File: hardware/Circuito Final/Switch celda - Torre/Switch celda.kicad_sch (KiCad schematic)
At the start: 28 parts, among them Q1 MMBT2222A, Q2 MMBT2907A, Q3 MMBT2222A

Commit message: Subida de la versión torrecita
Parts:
- removed J_In_Out_1: Conn_01x05_Socket, Connector_PinSocket_2.54mm:PinSocket_1x05_P2.54mm_Vertical, symbol Connector:Conn_01x05_Socket
- added J_In_Out_1: Conn_01x06_Socket, Connector_PinSocket_2.54mm:PinSocket_1x06_P2.54mm_Vertical, symbol Connector:Conn_01x06_Socket
- added TPgnd1, TPgnd2: TP_gnd, Connector_PinHeader_2.54mm:PinHeader_1x01_P2.54mm_Vertical, symbol Connector:TestPoint
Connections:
- net 0: now also J_In_Out_1.2 (Pin_2), J_In_Out_1.4 (Pin_4), TPgnd1.1, TPgnd2.1
- net Vcc: now also J_In_Out_1.5 (Pin_5)
- net Vcell_banco: now also J_In_Out_1.3 (Pin_3)
- net bus_neg: now also J_In_Out_1.1 (Pin_1)
- net bus_pos: now also J_In_Out_1.6 (Pin_6)

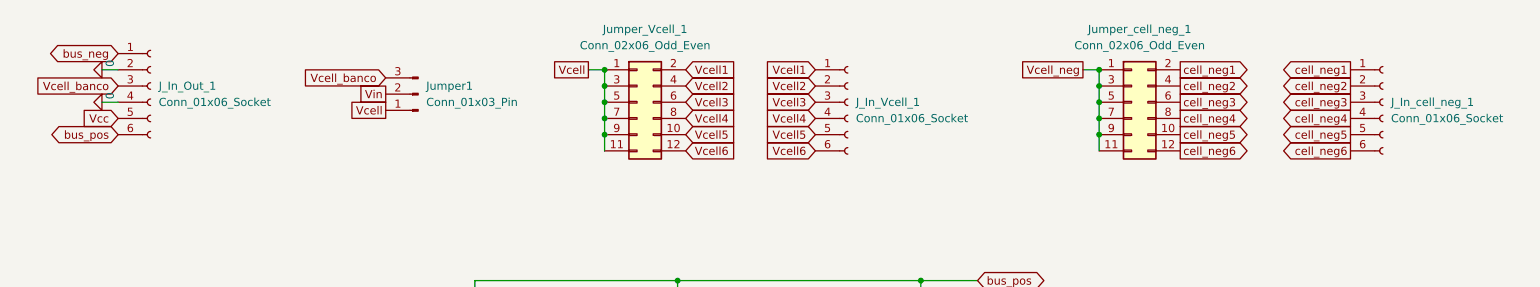
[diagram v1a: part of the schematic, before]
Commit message: Se duplican dos de las 3 tiras de pines del circuito de celda topología torre
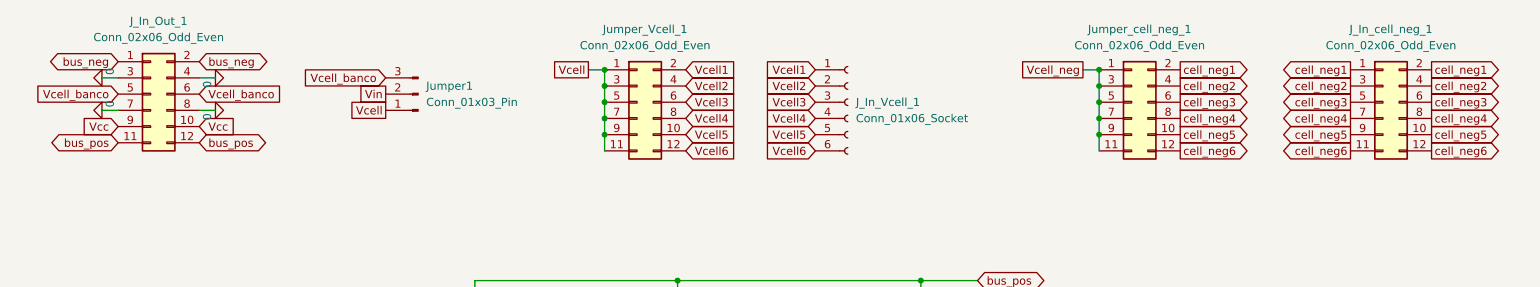
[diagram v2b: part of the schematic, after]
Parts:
- removed J_In_Out_1, J_In_cell_neg_1: Conn_01x06_Socket, Connector_PinSocket_2.54mm:PinSocket_1x06_P2.54mm_Vertical, symbol Connector:Conn_01x06_Socket
- added J_In_Out_1, J_In_cell_neg_1: Conn_02x06_Odd_Even, Connector_PinSocket_2.54mm:PinSocket_2x06_P2.54mm_Vertical, symbol Connector_Generic:Conn_02x06_Odd_Even
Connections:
- net 0: now also J_In_Out_1.3 (Pin_3), J_In_Out_1.4 (Pin_4), J_In_Out_1.7 (Pin_7), J_In_Out_1.8 (Pin_8)
- net Vcc: now also J_In_Out_1.10 (Pin_10), J_In_Out_1.9 (Pin_9)
- net Vcell_banco: now also J_In_Out_1.5 (Pin_5), J_In_Out_1.6 (Pin_6)
- net bus_neg: now also J_In_Out_1.1 (Pin_1), J_In_Out_1.2 (Pin_2)
- net bus_pos: now also J_In_Out_1.11 (Pin_11), J_In_Out_1.12 (Pin_12)
- net cell_neg1: now also J_In_cell_neg_1.1 (Pin_1), J_In_cell_neg_1.2 (Pin_2)
- net cell_neg2: now also J_In_cell_neg_1.3 (Pin_3), J_In_cell_neg_1.4 (Pin_4)
- net cell_neg3: now also J_In_cell_neg_1.5 (Pin_5), J_In_cell_neg_1.6 (Pin_6)
- net cell_neg4: now also J_In_cell_neg_1.7 (Pin_7), J_In_cell_neg_1.8 (Pin_8)
- net cell_neg5: now also J_In_cell_neg_1.10 (Pin_10), J_In_cell_neg_1.9 (Pin_9)
- net cell_neg6: now also J_In_cell_neg_1.11 (Pin_11), J_In_cell_neg_1.12 (Pin_12)

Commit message: Cambios al circuito de la celda en modo torre: clearance de 0.5mm (en lugar de la mínima), buses de potencia de 1.5mm (en lugar de 1mm) y resistores SMD de tamaño 1206 (en lugar de 0603)
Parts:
- F1: footprint Fuse:Fuse_0603_1608Metric_Pad1.05x0.95mm_HandSolder -> Fuse:Fuse_1206_3216Metric_Pad1.42x1.75mm_HandSolder
- R1, R2, R3, R4, R5, R6, RLED1, RLED2: footprint Resistor_SMD:R_0603_1608Metric_Pad0.98x0.95mm_HandSolder -> Resistor_SMD:R_1206_3216Metric_Pad1.30x1.75mm_HandSolder
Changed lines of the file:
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@@
 			)
 		)
-		(property "Footprint" "Resistor_SMD:R_0603_1608Metric_Pad0.98x0.95mm_HandSolder"
+		(property "Footprint" "Resistor_SMD:R_1206_3216Metric_Pad1.30x1.75mm_HandSolder"
 			(at 67.564 95.504 90)
 			(effects
@@
 			)
 		)
-		(property "Footprint" "Fuse:Fuse_0603_1608Metric_Pad1.05x0.95mm_HandSolder"
+		(property "Footprint" "Fuse:Fuse_1206_3216Metric_Pad1.42x1.75mm_HandSolder"
 			(at 156.21 63.5 0)
 			(effects
@@
 			)
 		)
-		(property "Footprint" "Resistor_SMD:R_0603_1608Metric_Pad0.98x0.95mm_HandSolder"
+		(property "Footprint" "Resistor_SMD:R_1206_3216Metric_Pad1.30x1.75mm_HandSolder"
 			(at 85.344 83.566 90)
 			(effects
@@
 			)
 		)
-		(property "Footprint" "Resistor_SMD:R_0603_1608Metric_Pad0.98x0.95mm_HandSolder"
+		(property "Footprint" "Resistor_SMD:R_1206_3216Metric_Pad1.30x1.75mm_HandSolder"
 			(at 85.344 64.516 90)
 			(effects
@@
 			)
 		)
-		(property "Footprint" "Resistor_SMD:R_0603_1608Metric_Pad0.98x0.95mm_HandSolder"
+		(property "Footprint" "Resistor_SMD:R_1206_3216Metric_Pad1.30x1.75mm_HandSolder"
 			(at 101.854 119.634 90)
 			(effects
@@
 			)
 		)
-		(property "Footprint" "Resistor_SMD:R_0603_1608Metric_Pad0.98x0.95mm_HandSolder"
+		(property "Footprint" "Resistor_SMD:R_1206_3216Metric_Pad1.30x1.75mm_HandSolder"
 			(at 214.884 100.584 90)
 			(effects
@@
 			)
 		)
-		(property "Footprint" "Resistor_SMD:R_0603_1608Metric_Pad0.98x0.95mm_HandSolder"
+		(property "Footprint" "Resistor_SMD:R_1206_3216Metric_Pad1.30x1.75mm_HandSolder"
 			(at 117.094 87.376 90)
 			(effects
@@
 			)
 		)
-		(property "Footprint" "Resistor_SMD:R_0603_1608Metric_Pad0.98x0.95mm_HandSolder"
+		(property "Footprint" "Resistor_SMD:R_1206_3216Metric_Pad1.30x1.75mm_HandSolder"
 			(at 227.584 89.916 90)
 			(effects
@@
 			)
 		)
-		(property "Footprint" "Resistor_SMD:R_0603_1608Metric_Pad0.98x0.95mm_HandSolder"
+		(property "Footprint" "Resistor_SMD:R_1206_3216Metric_Pad1.30x1.75mm_HandSolder"
 			(at 117.094 106.426 90)
 			(effects

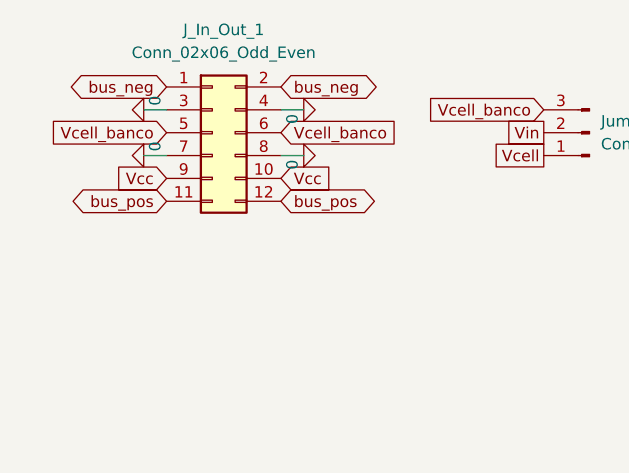
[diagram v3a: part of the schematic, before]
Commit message: Update menor de orden de señales en la entrada (VCC por bus_pos)
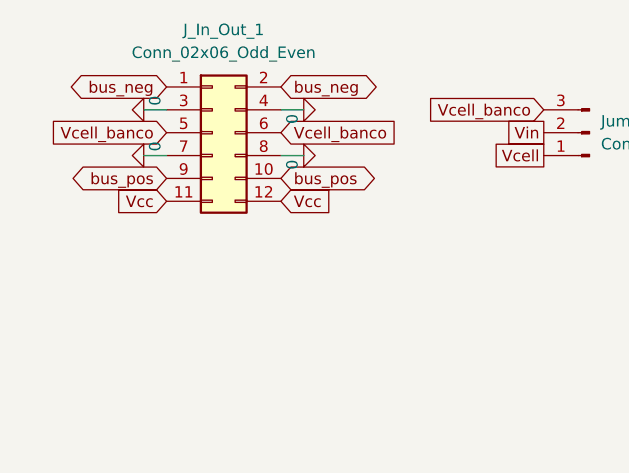
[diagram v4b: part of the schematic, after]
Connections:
- net Vcc: now also J_In_Out_1.11 (Pin_11), J_In_Out_1.12 (Pin_12); no longer J_In_Out_1.10 (Pin_10), J_In_Out_1.9 (Pin_9)
- net bus_pos: now also J_In_Out_1.10 (Pin_10), J_In_Out_1.9 (Pin_9); no longer J_In_Out_1.11 (Pin_11), J_In_Out_1.12 (Pin_12)
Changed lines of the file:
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@@
-		)
-	)
-	(global_label "Vcc"
-		(shape input)
-		(at 43.18 31.75 0)
-		(fields_autoplaced yes)
-		(effects
-			(font
-				(size 1.27 1.27)
-			)
-			(justify left)
-		)
-		(property "Intersheetrefs" "${INTERSHEET_REFS}"
-			(at 49.431 31.75 0)
-			(effects
-				(font
-					(size 1.27 1.27)
-				)
-				(justify left)
-				(hide yes)
-			)
 		)
 	)
@@
 				)
 				(justify left)
+				(hide yes)
+			)
+		)
+	)
+	(global_label "bus_pos"
+		(shape bidirectional)
+		(at 30.48 31.75 180)
+		(fields_autoplaced yes)
+		(effects
+			(font
+				(size 1.27 1.27)
+			)
+			(justify right)
+		)
+		(property "Intersheetrefs" "${INTERSHEET_REFS}"
+			(at 19.875 31.75 0)
+			(effects
+				(font
+					(size 1.27 1.27)
+				)
+				(justify right)
 				(hide yes)
 			)
@@
 		)
 	)
-	(global_label "bus_pos"
-		(shape bidirectional)
-		(at 30.48 34.29 180)
-		(fields_autoplaced yes)
-		(effects
-			(font
-				(size 1.27 1.27)
-			)
-			(justify right)
-		)
-		(property "Intersheetrefs" "${INTERSHEET_REFS}"
-			(at 19.875 34.29 0)
-			(effects
-				(font
-					(size 1.27 1.27)
-				)
-				(justify right)
-				(hide yes)
-			)
-		)
-	)
 	(global_label "Vcell2"
 		(shape input)
@@
 		)
 	)
+	(global_label "cell_neg1"
+		(shape output)
+		(at 196.85 22.86 0)
+		(fields_autoplaced yes)
+		(effects
+			(font
+				(size 1.27 1.27)
+			)
+			(justify left)
+		)
+		(property "Intersheetrefs" "${INTERSHEET_REFS}"
+			(at 208.9065 22.86 0)
+			(effects
+				(font
+					(size 1.27 1.27)
+				)
+				(justify left)
+				(hide yes)
+			)
+		)
+	)
+	(global_label "Vcell6"
+		(shape input)
+		(at 119.38 35.56 0)
+		(fields_autoplaced yes)
+		(effects
+			(font
+				(size 1.27 1.27)
+			)
+			(justify left)
+		)
+		(property "Intersheetrefs" "${INTERSHEET_REFS}"
+			(at 128.1709 35.56 0)
+			(effects
+				(font
+					(size 1.27 1.27)
+				)
+				(justify left)
+				(hide yes)
+			)
+		)
+	)
+	(global_label "Vcell1"
+		(shape input)
+		(at 139.7 22.86 180)
+		(fields_autoplaced yes)
+		(effects
+			(font
+				(size 1.27 1.27)
+			)
+			(justify right)
+		)
+		(property "Intersheetrefs" "${INTERSHEET_REFS}"
+			(at 130.9091 22.86 0)
+			(effects
+				(font
+					(size 1.27 1.27)
+				)
+				(justify right)
+				(hide yes)
+			)
+		)
+	)
+	(global_label "Vcell1"
+		(shape input)
+		(at 119.38 22.86 0)
+		(fields_autoplaced yes)
+		(effects
+			(font
+				(size 1.27 1.27)
+			)
+			(justify left)
+		)
+		(property "Intersheetrefs" "${INTERSHEET_REFS}"
+			(at 128.1709 22.86 0)
+			(effects
+				(font
+					(size 1.27 1.27)
+				)
+				(justify left)
+				(hide yes)
+			)
+		)
+	)
 	(global_label "Vcc"
 		(shape input)
-		(at 30.48 31.75 180)
-		(fields_autoplaced yes)
-		(effects
-			(font
-				(size 1.27 1.27)
-			)
-			(justify right)
-		)
-		(property "Intersheetrefs" "${INTERSHEET_REFS}"
-			(at 24.229 31.75 0)
-			(effects
-				(font
-					(size 1.27 1.27)
-				)
-				(justify right)
-				(hide yes)
-			)
-		)
-	)
-	(global_label "cell_neg1"
-		(shape output)
-		(at 196.85 22.86 0)
-		(fields_autoplaced yes)
-		(effects
-			(font
-				(size 1.27 1.27)
-			)
-			(justify left)
-		)
-		(property "Intersheetrefs" "${INTERSHEET_REFS}"
-			(at 208.9065 22.86 0)
-			(effects
-				(font
-					(size 1.27 1.27)
-				)
-				(justify left)
-				(hide yes)
-			)
-		)
-	)
-	(global_label "Vcell6"
-		(shape input)
-		(at 119.38 35.56 0)
-		(fields_autoplaced yes)
-		(effects
-			(font
-				(size 1.27 1.27)
-			)
-			(justify left)
-		)
-		(property "Intersheetrefs" "${INTERSHEET_REFS}"
-			(at 128.1709 35.56 0)
-			(effects
-				(font
-					(size 1.27 1.27)
-				)
-				(justify left)
-				(hide yes)
-			)
-		)
-	)
-	(global_label "Vcell1"
-		(shape input)
-		(at 139.7 22.86 180)
-		(fields_autoplaced yes)
-		(effects
-			(font
-				(size 1.27 1.27)
-			)
-			(justify right)
-		)
-		(property "Intersheetrefs" "${INTERSHEET_REFS}"
-			(at 130.9091 22.86 0)
-			(effects
-				(font
-					(size 1.27 1.27)
-				)
-				(justify right)
-				(hide yes)
-			)
-		)
-	)
-	(global_label "Vcell1"
-		(shape input)
-		(at 119.38 22.86 0)
-		(fields_autoplaced yes)
-		(effects
-			(font
-				(size 1.27 1.27)
-			)
-			(justify left)
-		)
-		(property "Intersheetrefs" "${INTERSHEET_REFS}"
-			(at 128.1709 22.86 0)
-			(effects
-				(font
-					(size 1.27 1.27)
-				)
-				(justify left)
-				(hide yes)
-			)
-		)
-	)
-	(global_label "bus_pos"
-		(shape bidirectional)
-		(at 43.18 34.29 0)
-		(fields_autoplaced yes)
-		(effects
-			(font
-				(size 1.27 1.27)
-			)
-			(justify left)
-		)
-		(property "Intersheetrefs" "${INTERSHEET_REFS}"
-			(at 54.8963 34.29 0)
-			(effects
-				(font
-					(size 1.27 1.27)
-				)
-				(justify left)
+		(at 30.48 34.29 180)
+		(fields_autoplaced yes)
+		(effects
+			(font
+				(size 1.27 1.27)
+			)
+			(justify right)
+		)
+		(property "Intersheetrefs" "${INTERSHEET_REFS}"
+			(at 24.229 34.29 0)
+			(effects
+				(font
+					(size 1.27 1.27)
+				)
+				(justify right)
 				(hide yes)
 			)
@@
 		)
 	)
+	(global_label "bus_pos"
+		(shape bidirectional)
+		(at 43.18 31.75 0)
+		(fields_autoplaced yes)
+		(effects
+			(font
+				(size 1.27 1.27)
+			)
+			(justify left)
+		)
+		(property "Intersheetrefs" "${INTERSHEET_REFS}"
+			(at 54.8963 31.75 0)
+			(effects
+				(font
+					(size 1.27 1.27)
+				)
+				(justify left)
+				(hide yes)
+			)
+		)
+	)
 	(global_label "Vcell_banco"
 		(shape input)
@@
 				(hide yes)
 			)
+		)
+	)
+	(global_label "Vcc"
+		(shape input)
+		(at 43.18 34.29 0)
+		(fields_autoplaced yes)
+		(effects
+			(font
+				(size 1.27 1.27)
+			)
+			(justify left)
+		)
+		(property "Intersheetrefs" "${INTERSHEET_REFS}"
+			(at 49.431 34.29 0)
+			(effects
+				(font
+					(size 1.27 1.27)
+				)
+				(justify left)
+				(hide yes)
+			)

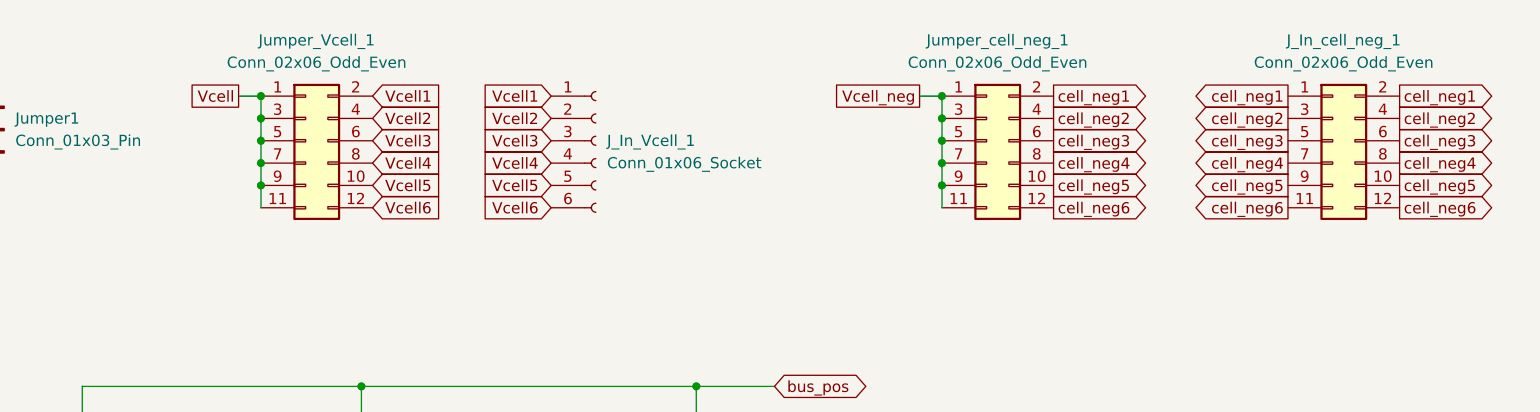
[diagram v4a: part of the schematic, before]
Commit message: Update switch celda: ahora tiene pines para conectarse con 7 celdas en lugar de 6
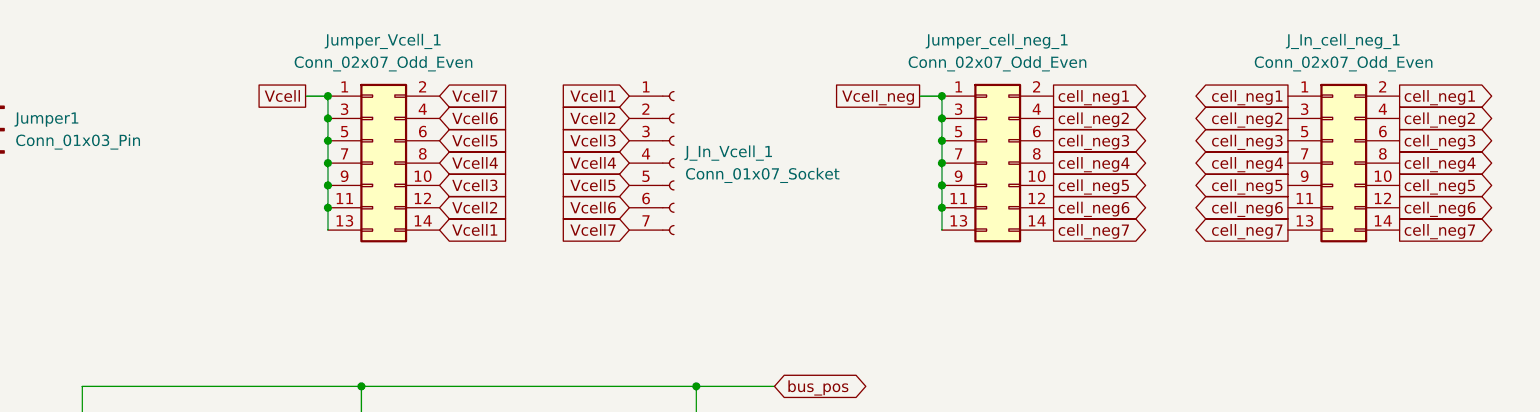
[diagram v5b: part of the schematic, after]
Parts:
- removed J_In_Vcell_1: Conn_01x06_Socket, Connector_PinSocket_2.54mm:PinSocket_1x06_P2.54mm_Vertical, symbol Connector:Conn_01x06_Socket
- removed J_In_cell_neg_1: Conn_02x06_Odd_Even, Connector_PinSocket_2.54mm:PinSocket_2x06_P2.54mm_Vertical, symbol Connector_Generic:Conn_02x06_Odd_Even
- removed Jumper_Vcell_1, Jumper_cell_neg_1: Conn_02x06_Odd_Even, Connector_PinHeader_2.54mm:PinHeader_2x06_P2.54mm_Vertical, symbol Connector_Generic:Conn_02x06_Odd_Even
- added J_In_Vcell_1: Conn_01x07_Socket, Connector_PinSocket_2.54mm:PinSocket_1x07_P2.54mm_Vertical, symbol Connector:Conn_01x07_Socket
- added J_In_cell_neg_1, Jumper_Vcell_1, Jumper_cell_neg_1: Conn_02x07_Odd_Even, Connector_PinSocket_2.54mm:PinSocket_2x07_P2.54mm_Vertical, symbol Connector_Generic:Conn_02x07_Odd_Even
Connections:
- net Vcell: now also Jumper_Vcell_1.1 (Pin_1), Jumper_Vcell_1.11 (Pin_11), Jumper_Vcell_1.13 (Pin_13), Jumper_Vcell_1.3 (Pin_3), Jumper_Vcell_1.5 (Pin_5), Jumper_Vcell_1.7 (Pin_7), Jumper_Vcell_1.9 (Pin_9)
- net Vcell1: now also J_In_Vcell_1.1 (Pin_1), Jumper_Vcell_1.14 (Pin_14)
- net Vcell2: now also J_In_Vcell_1.2 (Pin_2), Jumper_Vcell_1.12 (Pin_12)
- net Vcell3: now also J_In_Vcell_1.3 (Pin_3), Jumper_Vcell_1.10 (Pin_10)
- net Vcell4: now also J_In_Vcell_1.4 (Pin_4), Jumper_Vcell_1.8 (Pin_8)
- net Vcell5: now also J_In_Vcell_1.5 (Pin_5), Jumper_Vcell_1.6 (Pin_6)
- net Vcell6: now also J_In_Vcell_1.6 (Pin_6), Jumper_Vcell_1.4 (Pin_4)
- net Vcell_neg: now also Jumper_cell_neg_1.1 (Pin_1), Jumper_cell_neg_1.11 (Pin_11), Jumper_cell_neg_1.13 (Pin_13), Jumper_cell_neg_1.3 (Pin_3), Jumper_cell_neg_1.5 (Pin_5), Jumper_cell_neg_1.7 (Pin_7), Jumper_cell_neg_1.9 (Pin_9)
- net cell_neg1: now also J_In_cell_neg_1.1 (Pin_1), J_In_cell_neg_1.2 (Pin_2), Jumper_cell_neg_1.2 (Pin_2)
- net cell_neg2: now also J_In_cell_neg_1.3 (Pin_3), J_In_cell_neg_1.4 (Pin_4), Jumper_cell_neg_1.4 (Pin_4)
- net cell_neg3: now also J_In_cell_neg_1.5 (Pin_5), J_In_cell_neg_1.6 (Pin_6), Jumper_cell_neg_1.6 (Pin_6)
- net cell_neg4: now also J_In_cell_neg_1.7 (Pin_7), J_In_cell_neg_1.8 (Pin_8), Jumper_cell_neg_1.8 (Pin_8)
- net cell_neg5: now also J_In_cell_neg_1.10 (Pin_10), J_In_cell_neg_1.9 (Pin_9), Jumper_cell_neg_1.10 (Pin_10)
- net cell_neg6: now also J_In_cell_neg_1.11 (Pin_11), J_In_cell_neg_1.12 (Pin_12), Jumper_cell_neg_1.12 (Pin_12)
- new net Vcell7: J_In_Vcell_1.7 (Pin_7), Jumper_Vcell_1.2 (Pin_2)
- new net cell_neg7: J_In_cell_neg_1.13 (Pin_13), J_In_cell_neg_1.14 (Pin_14), Jumper_cell_neg_1.14 (Pin_14)
